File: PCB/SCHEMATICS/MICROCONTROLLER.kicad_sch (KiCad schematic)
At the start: 28 parts, among them IC1 CP2102-GMR, U6 C6482, U7 C6482

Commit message: Added footprints
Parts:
- C6: footprint (none) -> 0ohm:RESC1005X40N; PART  C4177 -> C17168; Unit Price 0.0012 -> 0.0005
- R25, R27: footprint (none) -> 2.2k:RESC1005X40N
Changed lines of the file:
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@@
       (effects (font (size 1.27 1.27)))
     )
-    (property "Footprint" "" (at 160.02 137.16 0)
+    (property "Footprint" "0ohm:RESC1005X40N" (at 160.02 137.16 0)
       (effects (font (size 1.27 1.27)) hide)
     )
@@
       (effects (font (size 1.27 1.27)) hide)
     )
-    (property "PART " "    C4177" (at 160.02 137.16 0)
-      (effects (font (size 1.27 1.27)) hide)
-    )
-    (property "Unit Price" "0.0012" (at 160.02 137.16 0)
+    (property "PART " "C17168" (at 160.02 137.16 0)
+      (effects (font (size 1.27 1.27)) hide)
+    )
+    (property "Unit Price" "0.0005" (at 160.02 137.16 0)
       (effects (font (size 1.27 1.27)) hide)
     )
@@
       (effects (font (size 1.27 1.27)))
     )
-    (property "Footprint" "" (at 203.2 53.34 0)
+    (property "Footprint" "0ohm:RESC1005X40N" (at 203.2 53.34 0)
       (effects (font (size 1.27 1.27)) hide)
     )
@@
       (effects (font (size 1.27 1.27)) hide)
     )
-    (property "PART " "    C4177" (at 203.2 53.34 0)
-      (effects (font (size 1.27 1.27)) hide)
-    )
-    (property "Unit Price" "0.0012" (at 203.2 53.34 0)
+    (property "PART " "C17168" (at 203.2 53.34 0)
+      (effects (font (size 1.27 1.27)) hide)
+    )
+    (property "Unit Price" "0.0005" (at 203.2 53.34 0)
       (effects (font (size 1.27 1.27)) hide)
     )
@@
       (effects (font (size 1.27 1.27)) (justify right))
     )
-    (property "Footprint" "" (at 41.91 95.504 0)
+    (property "Footprint" "0ohm:RESC1005X40N" (at 41.91 95.504 0)
       (effects (font (size 1.27 1.27)) hide)
     )
@@
       (effects (font (size 1.27 1.27)) hide)
     )
-    (property "PART " "    C4177" (at 41.91 95.504 0)
-      (effects (font (size 1.27 1.27)) hide)
-    )
-    (property "Unit Price" "0.0012" (at 41.91 95.504 0)
+    (property "PART " "C17168" (at 41.91 95.504 0)
+      (effects (font (size 1.27 1.27)) hide)
+    )
+    (property "Unit Price" "0.0005" (at 41.91 95.504 0)
       (effects (font (size 1.27 1.27)) hide)
     )
@@
       (effects (font (size 1.27 1.27)))
     )
-    (property "Footprint" "" (at 76.2 124.46 0)
+    (property "Footprint" "0ohm:RESC1005X40N" (at 76.2 124.46 0)
       (effects (font (size 1.27 1.27)) hide)
     )
@@
       (effects (font (size 1.27 1.27)) hide)
     )
-    (property "PART " "    C4177" (at 76.2 124.46 0)
-      (effects (font (size 1.27 1.27)) hide)
-    )
-    (property "Unit Price" "0.0012" (at 76.2 124.46 0)
+    (property "PART " "C17168" (at 76.2 124.46 0)
+      (effects (font (size 1.27 1.27)) hide)
+    )
+    (property "Unit Price" "0.0005" (at 76.2 124.46 0)
       (effects (font (size 1.27 1.27)) hide)
     )
@@
       (effects (font (size 1.27 1.27)))
     )
-    (property "Footprint" "" (at 185.42 53.34 0)
+    (property "Footprint" "2.2k:RESC1005X40N" (at 185.42 53.34 0)
       (effects (font (size 1.27 1.27)) hide)
     )
@@
       (effects (font (size 1.27 1.27)))
     )
-    (property "Footprint" "" (at 160.02 116.84 0)
+    (property "Footprint" "0ohm:RESC1005X40N" (at 160.02 116.84 0)
       (effects (font (size 1.27 1.27)) hide)
     )
@@
       (effects (font (size 1.27 1.27)) hide)
     )
-    (property "PART " "    C4177" (at 160.02 116.84 0)
-      (effects (font (size 1.27 1.27)) hide)
-    )
-    (property "Unit Price" "0.0012" (at 160.02 116.84 0)
+    (property "PART " "C17168" (at 160.02 116.84 0)
+      (effects (font (size 1.27 1.27)) hide)
+    )
+    (property "Unit Price" "0.0005" (at 160.02 116.84 0)
       (effects (font (size 1.27 1.27)) hide)
     )
@@
       (effects (font (size 1.27 1.27)))
     )
-    (property "Footprint" "" (at 76.2 121.92 0)
+    (property "Footprint" "0ohm:RESC1005X40N" (at 76.2 121.92 0)
       (effects (font (size 1.27 1.27)) hide)
     )
@@
       (effects (font (size 1.27 1.27)) hide)
     )
-    (property "PART " "    C4177" (at 76.2 121.92 0)
-      (effects (font (size 1.27 1.27)) hide)
-    )
-    (property "Unit Price" "0.0012" (at 76.2 121.92 0)
+    (property "PART " "C17168" (at 76.2 121.92 0)
+      (effects (font (size 1.27 1.27)) hide)
+    )
+    (property "Unit Price" "0.0005" (at 76.2 121.92 0)
       (effects (font (size 1.27 1.27)) hide)
     )
@@
       (effects (font (size 1.27 1.27)))
     )
-    (property "Footprint" "" (at 185.42 50.8 0)
+    (property "Footprint" "2.2k:RESC1005X40N" (at 185.42 50.8 0)
       (effects (font (size 1.27 1.27)) hide)
     )
@@
       (effects (font (size 1.27 1.27)))
     )
-    (property "Footprint" "" (at 203.2 50.8 0)
+    (property "Footprint" "0ohm:RESC1005X40N" (at 203.2 50.8 0)
       (effects (font (size 1.27 1.27)) hide)
     )
@@
       (effects (font (size 1.27 1.27)) hide)
     )
-    (property "PART " "    C4177" (at 203.2 50.8 0)
-      (effects (font (size 1.27 1.27)) hide)
-    )
-    (property "Unit Price" "0.0012" (at 203.2 50.8 0)
+    (property "PART " "C17168" (at 203.2 50.8 0)
+      (effects (font (size 1.27 1.27)) hide)
+    )
+    (property "Unit Price" "0.0005" (at 203.2 50.8 0)
       (effects (font (size 1.27 1.27)) hide)
     )
@@
       (effects (font (size 1.27 1.27)))
     )
-    (property "Footprint" "" (at 160.02 127 0)
+    (property "Footprint" "0ohm:RESC1005X40N" (at 160.02 127 0)
       (effects (font (size 1.27 1.27)) hide)
     )
@@
       (effects (font (size 1.27 1.27)) hide)
     )
-    (property "PART " "    C4177" (at 160.02 127 0)
-      (effects (font (size 1.27 1.27)) hide)
-    )
-    (property "Unit Price" "0.0012" (at 160.02 127 0)
-      (effects (font (size 1.27 1.27)) hide)
-    )
+    (property "PART " "C17168" (at 160.02 127 0)
+      (effects (font (size 1.27 1.27)) hide)
+    )
+    (property "Unit Price" "0.0005" (at 160.02 127 0)
+      (effects (font (size 1.27 1.27)) hide)
+    )

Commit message: Trying to merge
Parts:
- removed C6 (x3): 0, 0ohm:RESC1005X40N, symbol Device:R_Small_US
- removed C6: 3.3nF, symbol Device:C_Small
- removed D6, D7, D8: LED, symbol Device:LED
- removed IC1: CP2102-GMR, QFN50P500X500X100-29N-D, symbol DEBUGGER:CP2102-GMR
- removed MicroXNJ: ~, symbol DEBUGGER:Micro_usb
- removed TP34, TP35: TestPoint, symbol Connector:TestPoint
- removed U6, U7: C6482, symbol Memory_EEPROM:24LC08
- added C6 (x3): 0, symbol Device:R_Small_US
- added C8: 3.3nF, symbol Device:C_Small
- added IC1: CP2102-GMR, CP2102-GMR:QFN50P500X500X100-29N-D, symbol CP2102-GMR:CP2102-GMR
- added J1: MICROXNJ, MICROXNJ:SHOUHAN_MICROXNJ, symbol MICROXNJ:MICROXNJ
- added LED1: KT-0603R, KT-0603R:LEDC1608X70N, symbol KT-0603R:KT-0603R
- added LED2, LED3: KT-0603R, LEDC1608X70N, symbol KT-0603R:KT-0603R
- added TP36, TP37: TestPoint, symbol Connector:TestPoint
- added U6, U7: AT24C256C-SSHL-T, AT24C256C-SSHL-T:SOIC127P600X175-8N, symbol AT24C256C-SSHL-T:AT24C256C-SSHL-T
- C6: footprint 0ohm:RESC1005X40N -> (none); PART  C17168 -> C4177; Unit Price 0.0005 -> 0.0012
- R25, R27: footprint 2.2k:RESC1005X40N -> (none)
- TP26, TP32, TP33: PART  TP26 -> TP27
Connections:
- net 3V3: now also C6.1, IC1.6 (VDD)
- net 5V: now also IC1.8 (VBUS), J1.1 (VBUS)
- net D+: now also IC1.4 (D+)
- net D-: now also IC1.5 (D-)
- net GND: now also C8.2, IC1.3 (GND), J1.4 (ID), J1.5 (GND), J1.S1 (SHIELD), J1.S2 (SHIELD), J1.S3 (SHIELD), J1.S4 (SHIELD), J1.S5 (SHIELD), J1.S6 (SHIELD), LED1.1 (K), LED2.1 (K), LED3.1 (K), U6.1 (A0), U6.2 (A1), U6.3 (A2), U6.4 (GND), U7.1 (A0), U7.2 (A1), U7.3 (A2), U7.4 (GND)
- net PA10: now also C6.2, IC1.25 (RXD)
- net PA9: now also C6.2, IC1.26 (TXD)
- net at C6.1: now also LED3.2 (A)
- net at TP26.1: now also U7.7 (WP)
- net at TP27.1: now also U7.8 (VCC)
- net at TP25.1: now also C6.2, U6.8 (VCC)
- net at R25.1, TP23.1: now also J1.3 (D+)
- net at R27.1, TP24.1: now also J1.2 (D-)
- net at C6.1: now also LED1.2 (A)
- net at TP33.1: now also U7.5 (SDA)
- net at TP32.1: now also U7.6 (SCL)
- net at C6.1: now also LED2.2 (A)
- new net: C6.1, TP36.1, U6.6 (SCL)
- new net: C6.1, TP37.1, U6.5 (SDA)
- new net: C8.1, U6.7 (WP)
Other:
- moved on the sheet: C6, TP22, TP25

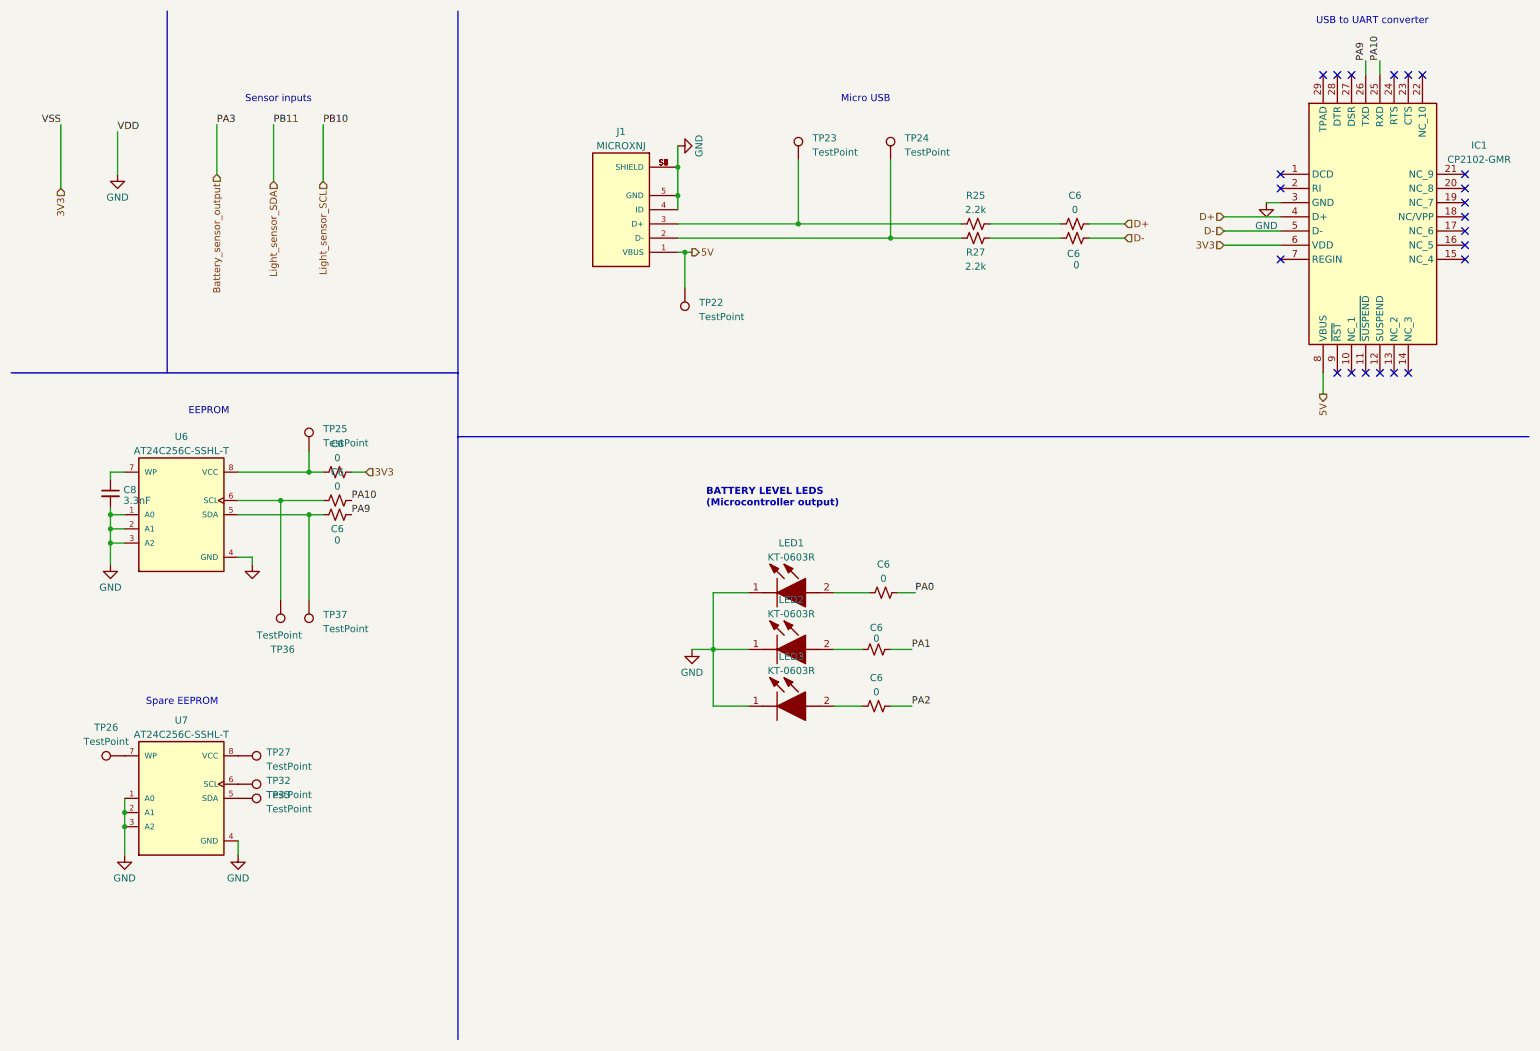
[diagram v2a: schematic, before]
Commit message: updated schematics and footprints
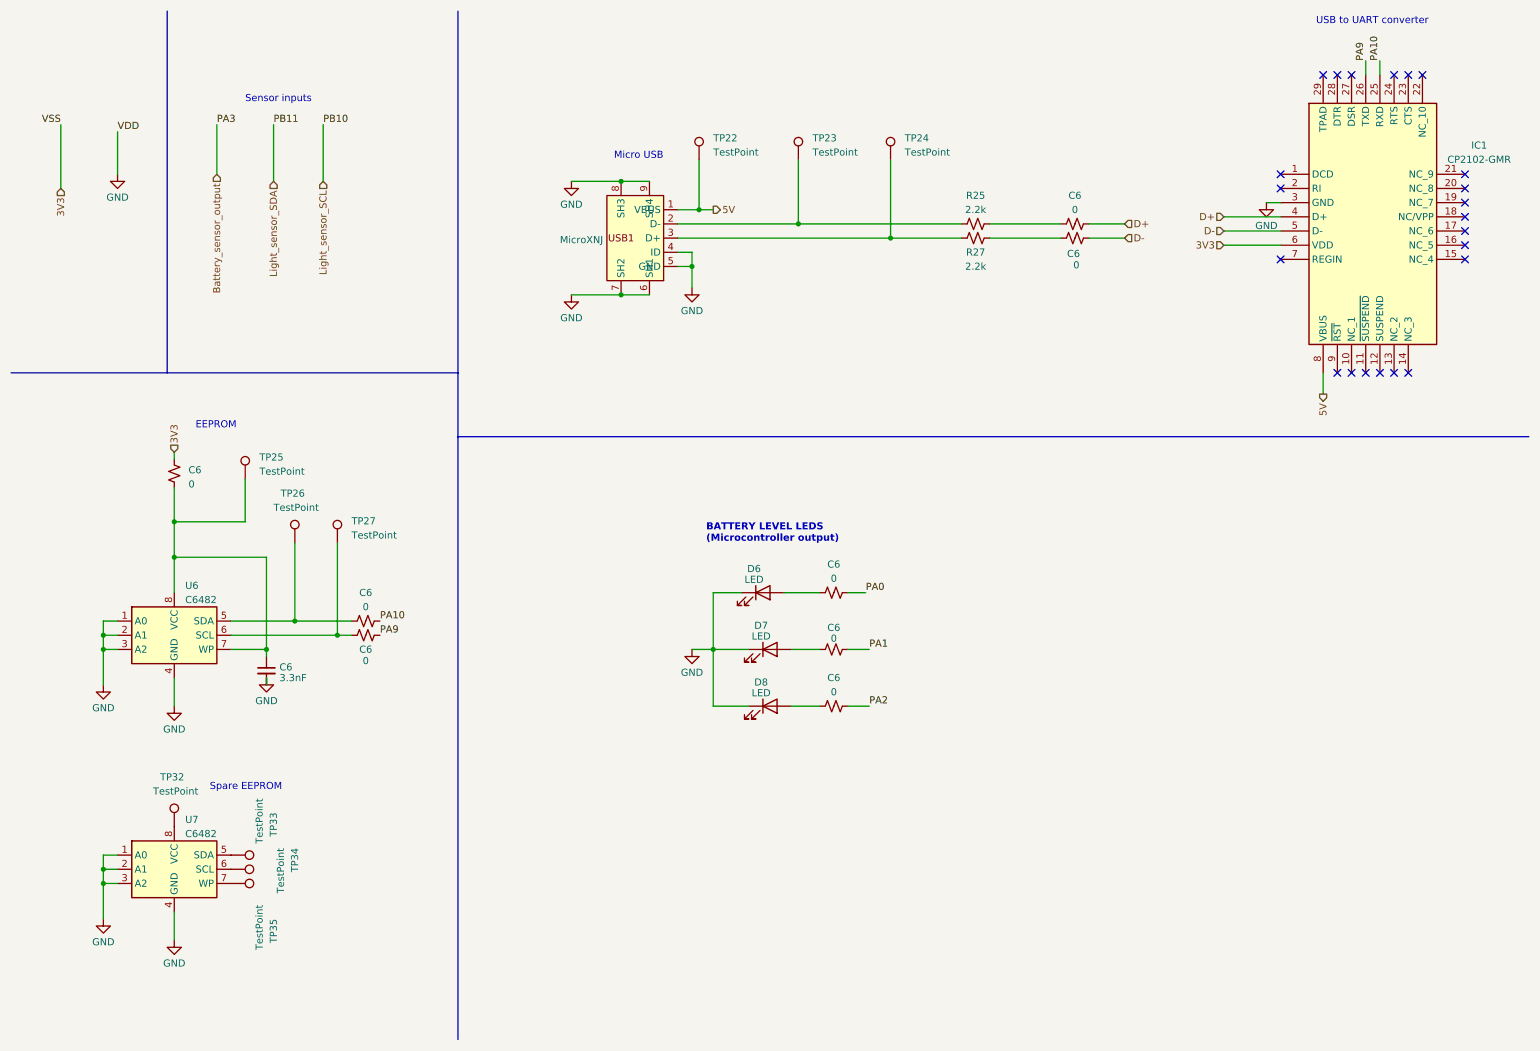
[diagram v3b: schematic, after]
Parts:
- removed C6 (x3): 0, symbol Device:R_Small_US
- removed C8: 3.3nF, symbol Device:C_Small
- removed IC1: CP2102-GMR, CP2102-GMR:QFN50P500X500X100-29N-D, symbol CP2102-GMR:CP2102-GMR
- removed J1: MICROXNJ, MICROXNJ:SHOUHAN_MICROXNJ, symbol MICROXNJ:MICROXNJ
- removed LED1: KT-0603R, KT-0603R:LEDC1608X70N, symbol KT-0603R:KT-0603R
- removed LED2, LED3: KT-0603R, LEDC1608X70N, symbol KT-0603R:KT-0603R
- removed TP36, TP37: TestPoint, symbol Connector:TestPoint
- removed U6, U7: AT24C256C-SSHL-T, AT24C256C-SSHL-T:SOIC127P600X175-8N, symbol AT24C256C-SSHL-T:AT24C256C-SSHL-T
- added C6 (x3): 0, 0ohm:RESC1005X40N, symbol Device:R_Small_US
- added C6: 3.3nF, footprint:C0603, symbol Device:C_Small
- added D6, D7, D8: LED, footprint:LED0603-RD, symbol Device:LED
- added IC1: CP2102-GMR, footprint:WQFN-28_L5.0-W5.0-P0.50-BL-EP3.2, symbol DEBUGGER:CP2102-GMR
- added MicroXNJ: ~, footprint:MICRO-USB-SMD_MICROXNJ, symbol DEBUGGER:Micro_usb
- added TP34, TP35: TestPoint, symbol Connector:TestPoint
- added U6, U7: C6482, footprint:SOIC-8_L4.9-W3.9-P1.27-LS6.0-BL, symbol Memory_EEPROM:24LC08
- C6: footprint (none) -> 0ohm:RESC1005X40N; PART  C4177 -> C17168; Unit Price 0.0012 -> 0.0005
- R25, R27: footprint (none) -> 2.2k:RESC1005X40N
- TP26, TP32, TP33: PART  TP27 -> TP26
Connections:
- net 3V3: now also C6.2, IC1.6 (VDD)
- net 5V: now also IC1.8 (VBUS), MicroXNJ.1 (VBUS)
- net D+: now also IC1.4 (D+)
- net D-: now also IC1.5 (D-)
- net GND: now also C6.2, D6.1 (K), D7.1 (K), D8.1 (K), IC1.3 (GND), MicroXNJ.4 (ID), MicroXNJ.5 (GND), MicroXNJ.6 (SH1), MicroXNJ.7 (SH2), MicroXNJ.8 (SH3), MicroXNJ.9 (SH4), U6.1 (A0), U6.2 (A1), U6.3 (A2), U6.4 (GND), U7.1 (A0), U7.2 (A1), U7.3 (A2), U7.4 (GND)
- net PA10: now also C6.2, IC1.25 (RXD)
- net PA9: now also C6.2, IC1.26 (TXD)
- net at C6.1: now also D8.2 (A)
- net at R25.1, TP23.1: now also MicroXNJ.2 (D-)
- net at R27.1, TP24.1: now also MicroXNJ.3 (D+)
- net at C6.1: now also D6.2 (A)
- net at TP33.1: now also U7.5 (SDA)
- net at TP32.1: now also U7.8 (VCC)
- net at TP26.1: now also C6.1, U6.5 (SDA)
- net at TP27.1: now also C6.1, U6.6 (SCL)
- net at TP25.1: now also C6.1, C6.1, U6.7 (WP), U6.8 (VCC)
- net at C6.1: now also D7.2 (A)
- new net: TP34.1, U7.6 (SCL)
- new net: TP35.1, U7.7 (WP)
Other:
- moved on the sheet: C6, TP22, TP25

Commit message: Updating schematics
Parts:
- added U8: ~, footprints:STM32F051C6T6, symbol UCT:STM32F051C6TG6_Target
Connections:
- net 3V3: now also U8.1 (VBAT), U8.24 (V+), U8.48 (V+), U8.9 (V+)
- net Battery_sensor_output: now also U8.13 (PA3)
- net GND: now also U8.23 (GND), U8.47 (GND), U8.8 (GND)
- net Light_sensor_SCL: now also U8.21 (PB10)
- net Light_sensor_SDA: now also U8.22 (PB11)
- net PA0: now also U8.10 (PA0)
- net PA1: now also U8.11 (PA1)
- net PA10: now also U8.31 (PA10); no longer IC1.25 (RXD)
- net PA2: now also U8.12 (PA2)
- net PA9: now also U8.30 (PA9); no longer IC1.26 (TXD)
- new net PA11: IC1.26 (TXD), U8.32 (PA11)
- new net PA12: IC1.25 (RXD), U8.33 (PA12)
- no-connect marks 22 -> 53
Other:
- note added: "STM32 Note: this is not on the HAT, this symbol represents the footprint for headers to be soldered onto"
- moved on the sheet: C6, D6, D7, D8
